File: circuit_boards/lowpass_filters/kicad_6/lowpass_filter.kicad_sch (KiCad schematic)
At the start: 48 parts, among them Q10 BCM847, Q11 BCM847, Q12 BCM847, Q13 BCM847, Q14 BCM847, Q15 BCM847, Q16 BCM847, Q17 MMBT3906, Q18 MMBT3904, U1 TL072

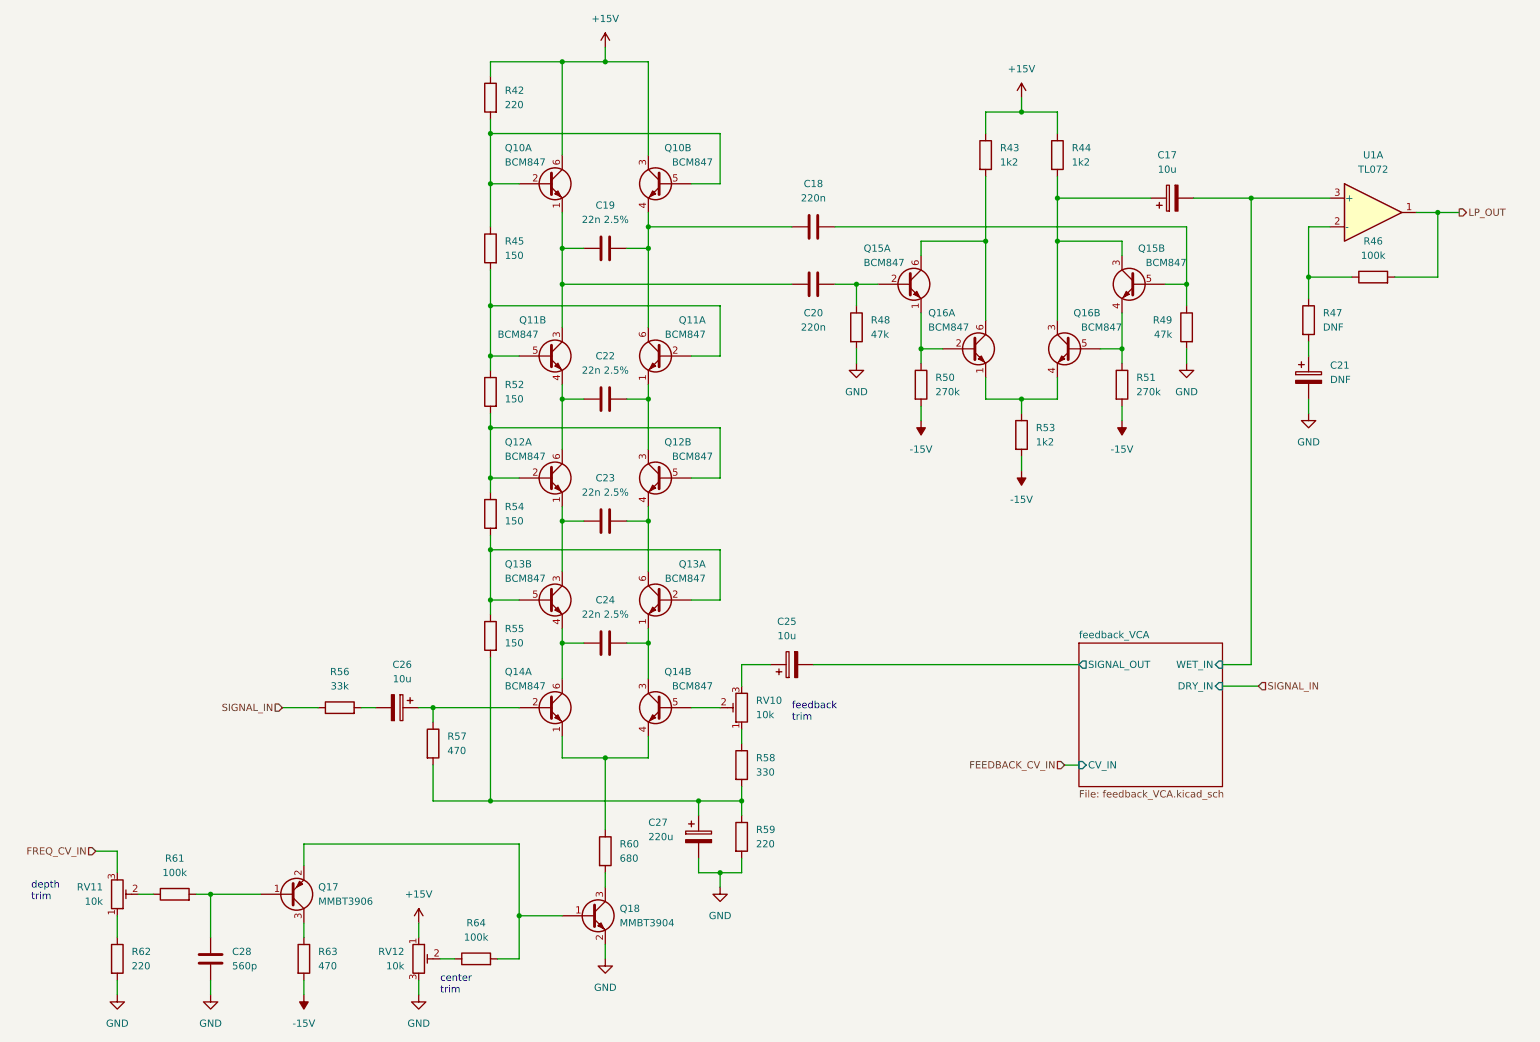
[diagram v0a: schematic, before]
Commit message: Update PCB files, fix VCF mix polarity
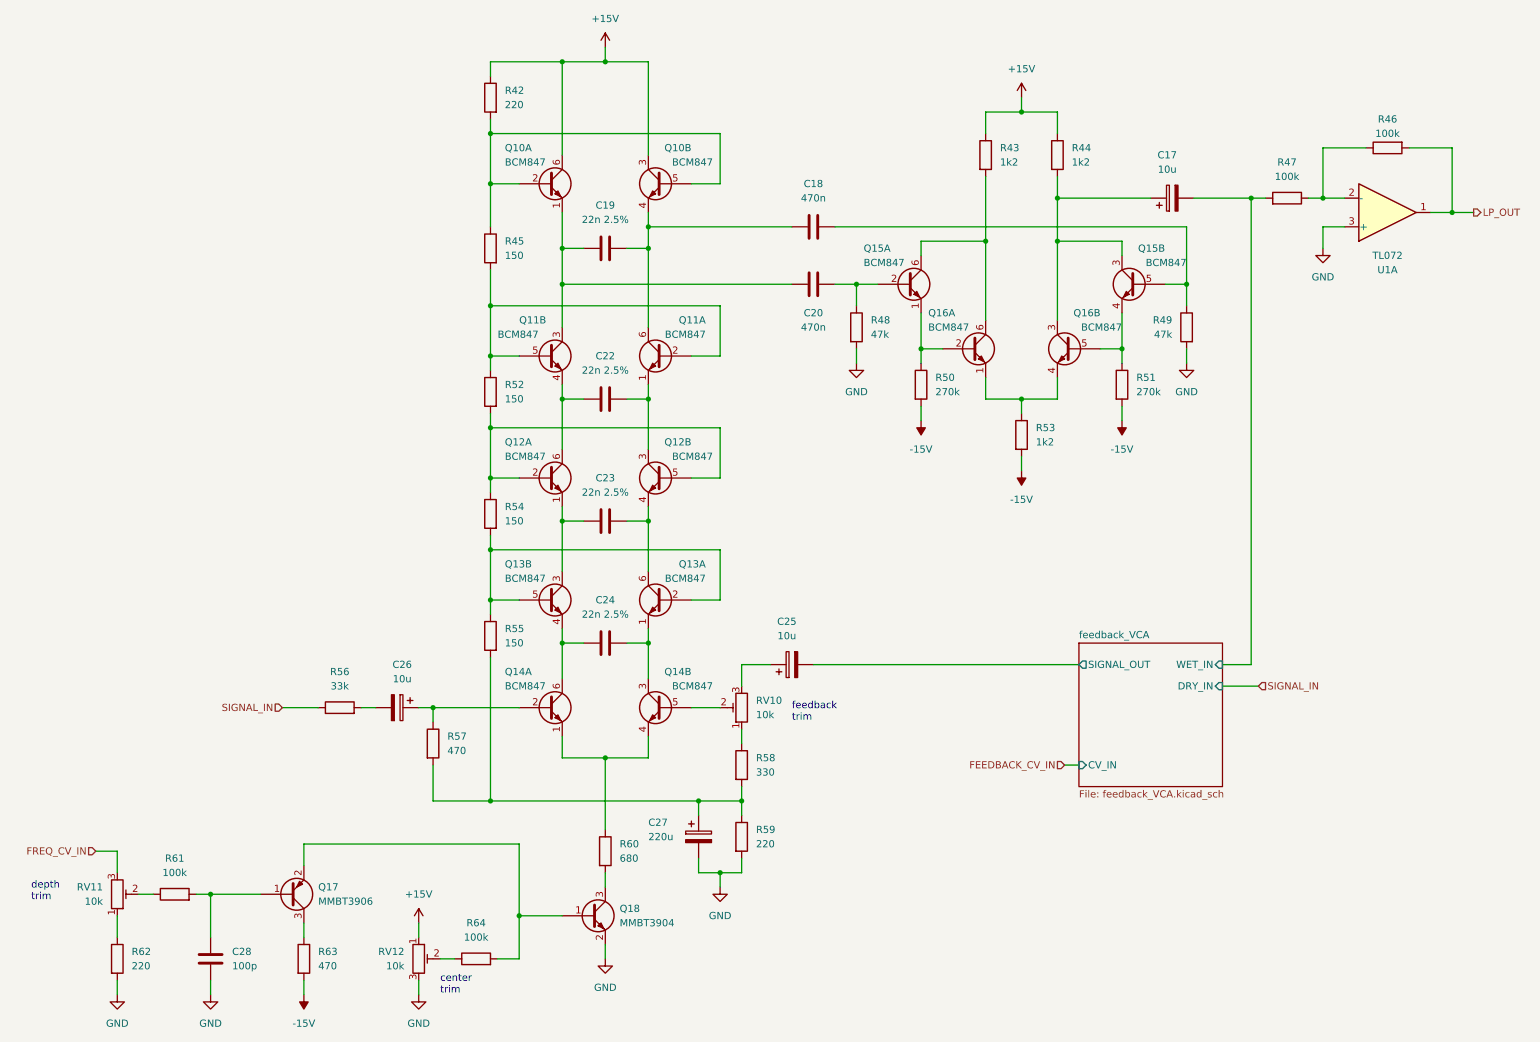
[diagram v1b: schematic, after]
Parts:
- removed C21: DNF, Capacitor_THT:CP_Radial_D6.3mm_P2.50mm, symbol Device:C_Polarized
- C18, C20: value 220n -> 470n
- C28: value 560p -> 100p
- R47: value DNF -> 100k
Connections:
- net GND: now also U1.3 (+)
- net feedback_VCA/WET_IN: now also R47.2; no longer U1.3 (+)
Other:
- moved on the sheet: R46, R47, U1A
